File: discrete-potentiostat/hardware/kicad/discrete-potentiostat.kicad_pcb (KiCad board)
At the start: 6 copper layers, 26 x 24 mm, 70 parts, among them J1 ELECTRODES, J2 SWD, U1 BQ51013BRHLR, U2 MIC5205-3.3YM5, U3 nRF52832-QFAA, U4 OPA2391DGKR, U5 REF35102QDBVR, U6 MCP73832T-2ACI/OT, Y1 32MHz 8pF 10ppm

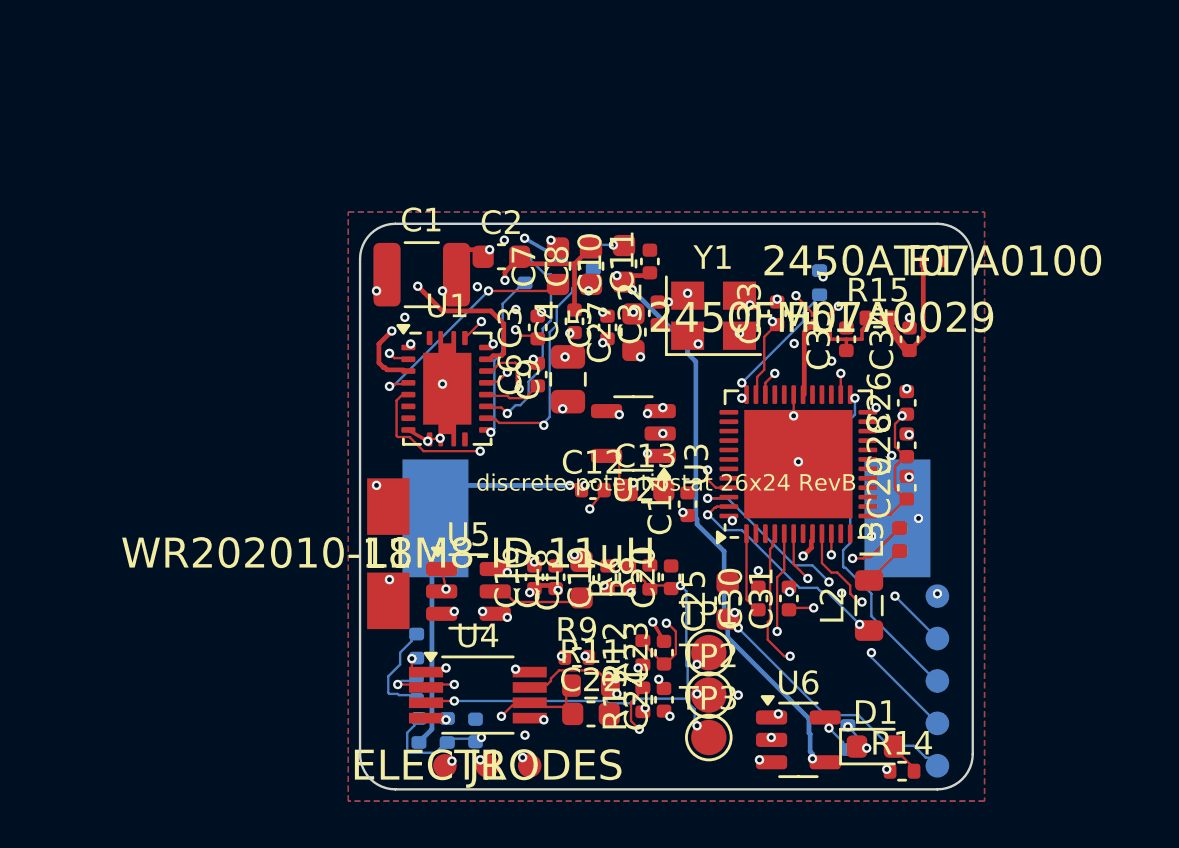
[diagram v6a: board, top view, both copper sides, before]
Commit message: Shrink board to 23.4x22mm (RevC, -17.5%); 4-layer ruled out
Size floor analysis: width bound by LIR2032 tab pads (+/-9.8mm + pad +
edge), height by the O21 cell zone -> 23.4x22 is the practical minimum
without changing the battery/tab structure.

- RevC placement: ICs on top; back reduced to 4 corner pockets (R1/R2/
  TH1, R3, R5/R6/C15); J2 SWD pads + TP1-3 moved to the front right
  column (clears the battery, easier soldering); DCDC inductors L2/L3
  relocated next to U3.46/47 (fixed the persistent DCC/DEC4 congestion);
  C30 rotated 180deg so DEC1 faces the open channel
- Routing: auto-route + priority/rip convergence to 4 links, then
  validated hand paths (close4.py): DCC via-in-pad U3.47 -> B detour ->
  via in L2.1; CLAMP2 B diagonal; DEC1 In3 + via-in-pad C30.1; ADC_P
  all-front channel route; +BATT/AFE_PWR/COMM1 local reroutes for GND
  orphan stitching
- Final DRC: 0 unconnected, 0 clearance, 0 hole, 0 edge, 0 isolated
- 4-layer experiment (same placement, 3 routing layers): fresh, priority
  and AGGRO strategies all plateau at 12-22 unconnected pads -> 6-layer
  stays; conclusion documented in kicad/README
- generator: gen_pcb.py is now the RevC generator (LAYERS4=1 for the 4L
  variant; legalize before RF pre-route), route_pcb.py gains PRIORITY/
  BOARD_W/H envs + 4L layer map fix; new gnd_fix_auto.py, finish_links.py,
  close4.py

Co-Authored-By: Claude Fable 5 <noreply@anthropic.com>
Claude-Session: https://claude.ai/code/session_01GUNJUwfGKqvkZFmTaLQRu3
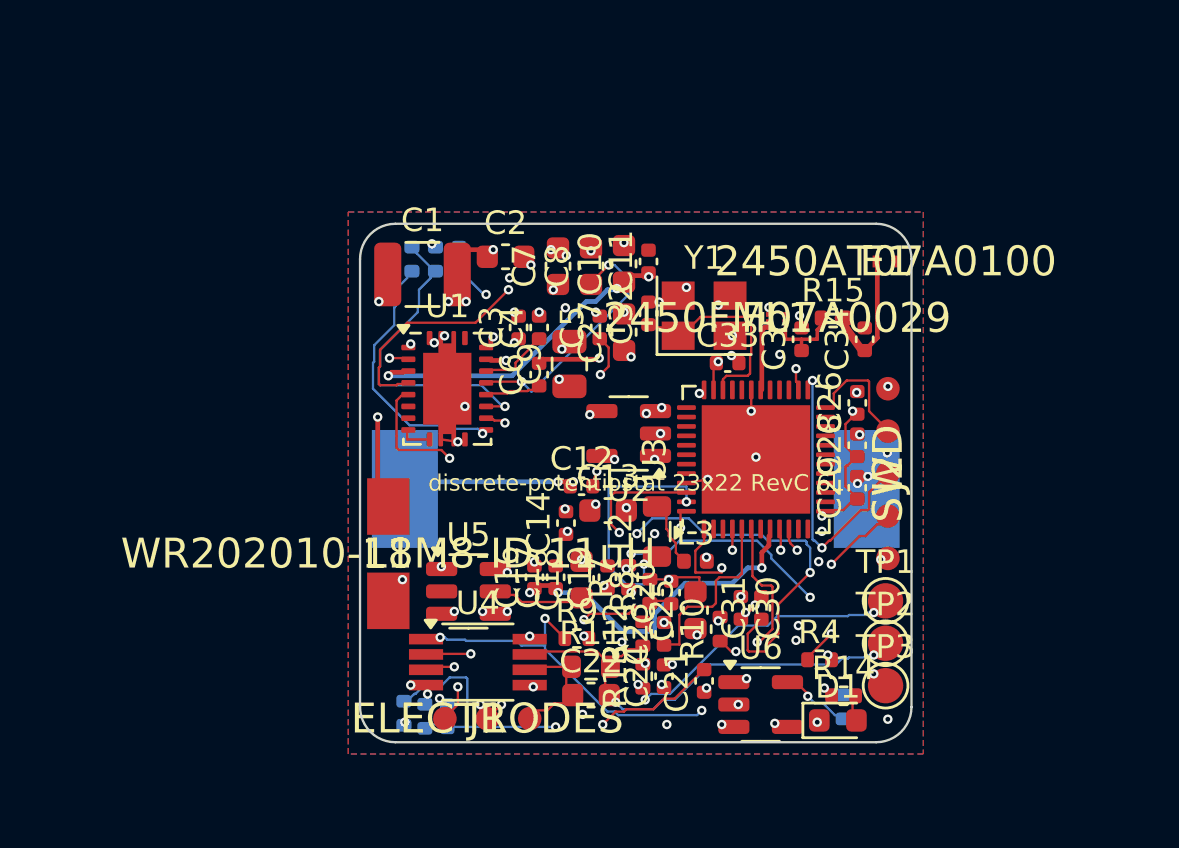
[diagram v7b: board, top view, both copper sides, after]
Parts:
- C21, J2, R10, R4: moved to F.Cu
- moved R4 16.0 mm to (119.5, 118.5), turned to 0 degrees
- moved R10 12.9 mm to (115.3, 117.2)
- moved C21 12.2 mm to (114.6, 119.4)
- moved L2 9.53 mm to (112.6, 113.1)
- moved J2 9.05 mm to (122.4, 110.6)
- moved L3 8.72 mm to (114.2, 114.3), turned to 0 degrees
- moved TP1 7.82 mm to (122.3, 116.0)
- moved TP2 7.82 mm to (122.3, 117.8)
- moved TP3 7.82 mm to (122.3, 119.6)
- moved TH1 5.70 mm to (104.2, 101.5)
- moved R2 5.32 mm to (103.2, 101.5)
- moved C14 5.22 mm to (108.7, 112.7)
- moved R1 4.83 mm to (102.2, 101.5)
- moved R14 4.05 mm to (120.5, 120.0)
- moved C33 2.98 mm to (115.6, 105.9), turned to 0 degrees
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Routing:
- net CE_AMP: track 5.83 -> 18.5 mm, vias 3 -> 4
- net CHG_N: track 20.9 -> 8.89 mm, vias 3 -> 4
- net RECT: track 15.0 -> 3.23 mm
- net DEC4: track 13.1 -> 24.3 mm
- net VBIAS: track 18.5 -> 27.5 mm, vias 3 -> 6
- net RE: track 5.55 -> 13.9 mm, vias 3 -> 4
- net TIA_OUT: track 8.26 -> 16.5 mm, vias 4 -> 2
- net VREF: track 17.3 -> 25.0 mm, vias 6 -> 7
- net ADC_N: track 15.8 -> 8.30 mm
- net +BATT: track 34.6 -> 41.4 mm, vias 7 -> 9
- net ADC_P: track 14.7 -> 8.04 mm, vias 3 -> 0
- net +3V3: track 44.7 -> 38.5 mm, vias 7 -> 10
- net NRST: track 10.6 -> 4.31 mm, vias 2 -> 0
- net V5OUT: track 38.2 -> 33.7 mm
- net CLAMP2: track 5.86 -> 10.4 mm
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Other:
- board size 26 x 24 mm -> 23.4 x 22 mm
- board text added: "discrete-potentiostat 23x22 RevC 6L"
- board text removed: "discrete-potentiostat 26x24 RevB"

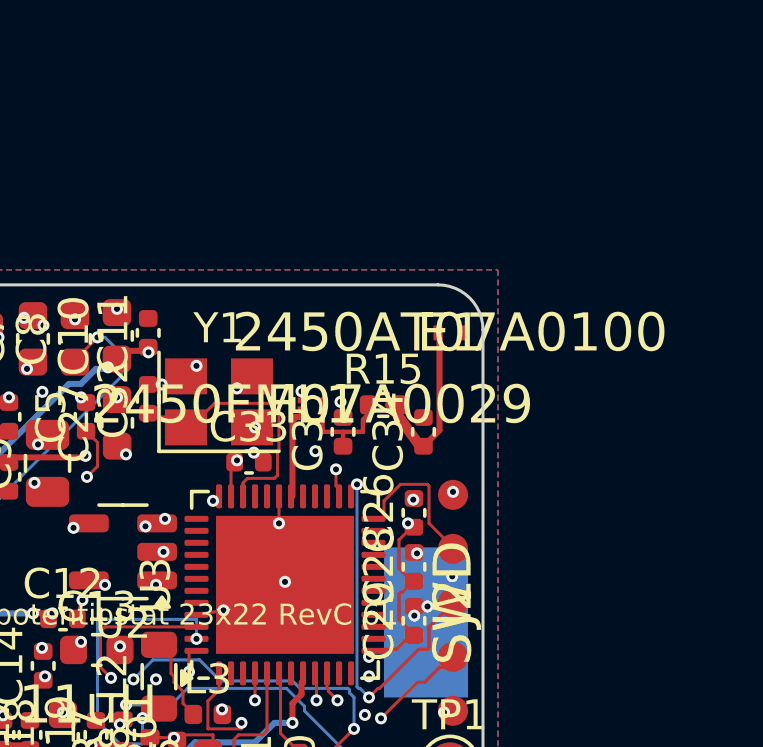
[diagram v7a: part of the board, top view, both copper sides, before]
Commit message: Fix E1 antenna to datasheet-true 4-terminal land pattern (GND connected)
Johanson 2450AT07A0100 datasheet (36S0021A Rev 4.1) defines 4 terminals:
1/4 = Feed, 2/3 = GND. Previous footprint was a wrong 2-pad guess with
the GND end floating.

- gen_pcb.py: 4-pad footprint (0.3x0.25 pads, rows +-0.3 along L,
  columns +-0.175 across W per eval-board land pattern); E1 moved to
  (19.4, 0.95) rot 270 - vertical edge mount, GND row toward top edge;
  parametric feed bridge to R15.2 and 0.3mm GND strip into left F pour
- gen_sch.py: custom 4-pin antenna symbol (1/4 ANT_FEED, 2/3 GND);
  netlist check PASS (47 nets)
- Board file: live surgery applied (new E1 + feed bridge + GND strip,
  old 2-pad E1 and stub removed); DRC re-verified - zero copper
  violations (unconnected 0, clearance 0)
- Schematic/PDFs regenerated; bom.md and kicad/README.md updated

Co-Authored-By: Claude Fable 5 <noreply@anthropic.com>
Claude-Session: https://claude.ai/code/session_01GUNJUwfGKqvkZFmTaLQRu3
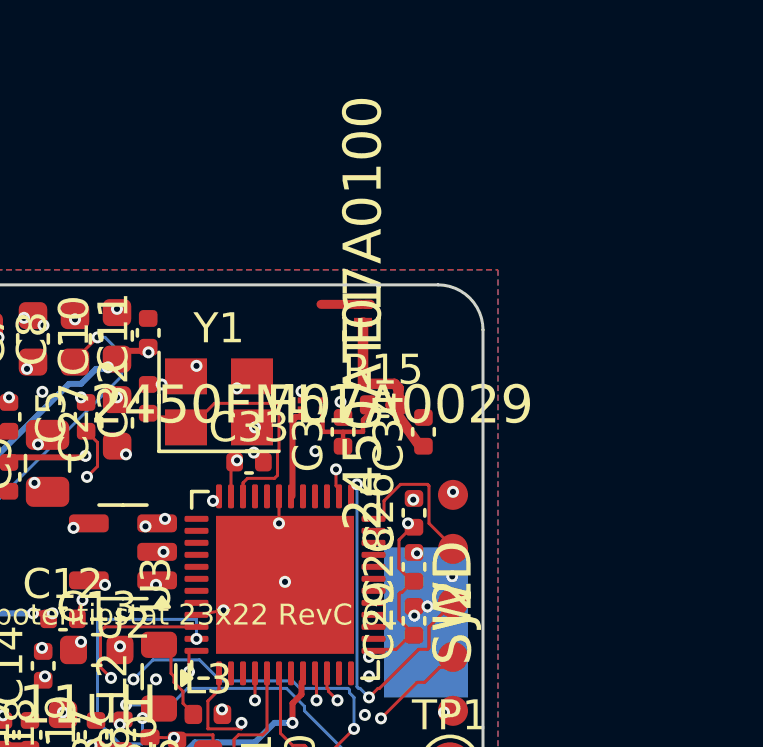
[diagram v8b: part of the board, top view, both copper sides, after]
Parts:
- moved E1 2.97 mm to (119.4, 101.0), turned to -90 degrees
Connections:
- E1 pad 2: (no net) -> GND
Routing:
- net GND: track 16.8 -> 18.4 mm
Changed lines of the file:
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@@
     )
   )
-  (footprint "pstat:Johanson_2450AT07A0100" (layer "F.Cu")
-    (at 122.3 101.6)
-    (fp_text reference "E1" (at 0 0) (layer "F.SilkS")
-        (effects (font (size 1.27 1.27) (thickness 0.15)))
-    )
-    (fp_text value "2450AT07A0100" (at 0 0) (layer "F.SilkS")
-        (effects (font (size 1.27 1.27) (thickness 0.15)))
-    )
-    (pad "1" smd rect (at -0.4 0) (size 0.3 0.5) (layers "F.Cu" "F.Paste" "F.Mask")
-      (net 10 "ANT_FEED") (thermal_bridge_angle 45))
-    (pad "2" smd rect (at 0.4 0) (size 0.3 0.5) (layers "F.Cu" "F.Paste" "F.Mask")
-      (thermal_bridge_angle 45))
-  )
   (footprint "C_0402_1005Metric" (layer "F.Cu")
     (at 121.1 109.4 90)
@@
     )
   )
+  (footprint "pstat:Johanson_2450AT07A0100" (layer "F.Cu")
+    (at 119.4 100.95 -90)
+    (fp_text reference "E1" (at 0 0 -90) (layer "F.SilkS")
+        (effects (font (size 1.27 1.27) (thickness 0.15)))
+    )
+    (fp_text value "2450AT07A0100" (at 0 0 -90) (layer "F.SilkS")
+        (effects (font (size 1.27 1.27) (thickness 0.15)))
+    )
+    (pad "1" smd rect (at 0.3 -0.175 270) (size 0.3 0.25) (layers "F.Cu" "F.Paste" "F.Mask")
+      (net 10 "ANT_FEED") (thermal_bridge_angle 45))
+    (pad "2" smd rect (at -0.3 -0.175 270) (size 0.3 0.25) (layers "F.Cu" "F.Paste" "F.Mask")
+      (net 28 "GND") (thermal_bridge_angle 45))
+    (pad "3" smd rect (at -0.3 0.175 270) (size 0.3 0.25) (layers "F.Cu" "F.Paste" "F.Mask")
+      (net 28 "GND") (thermal_bridge_angle 45))
+    (pad "4" smd rect (at 0.3 0.175 270) (size 0.3 0.25) (layers "F.Cu" "F.Paste" "F.Mask")
+      (net 10 "ANT_FEED") (thermal_bridge_angle 45))
+  )
   (footprint "pstat:Johanson_0402_4pin" (layer "F.Cu")
     (at 117.7 104)
@@
   (segment (start 118.735 105.38) (end 118.735 104.9) (width 0.15) (layer "F.Cu") (net 9))
   (segment (start 118.05 104.9) (end 119.4 104.9) (width 0.15) (layer "F.Cu") (net 9))
+  (segment (start 120.45 103.3) (end 120.585 103.44) (width 0.35) (layer "F.Cu") (net 10))
+  (segment (start 120.585 103.44) (end 120.585 103.9) (width 0.35) (layer "F.Cu") (net 10))
   (segment (start 120.31 104) (end 121.3 105.38) (width 0.35) (layer "F.Cu") (net 10))
-  (segment (start 121.95 104.845) (end 121.95 101.6) (width 0.2) (layer "F.Cu") (net 10))
-  (segment (start 121.415 105.38) (end 121.95 104.845) (width 0.2) (layer "F.Cu") (net 10))
+  (segment (start 119.4 103.3) (end 120.45 103.3) (width 0.35) (layer "F.Cu") (net 10))
+  (segment (start 119.4 101.25) (end 119.4 103.3) (width 0.35) (layer "F.Cu") (net 10))
   (segment (start 101.25 105.7) (end 101.85 105.7) (width 0.1) (layer "F.Cu") (net 11))
   (via (at 106.55 105.05) (size 0.4) (drill 0.2) (layers "F.Cu" "B.Cu") (net 11))
@@
   (segment (start 112.24 103.32) (end 112.69 103.32) (width 0.15) (layer "F.Cu") (net 28))
   (segment (start 111.299999 112.17) (end 111.3 112.05) (width 0.1) (layer "F.Cu") (net 28))
+  (segment (start 119.65 100.65) (end 118 100.65) (width 0.3) (layer "F.Cu") (net 28))
   (segment (start 103.4625 114.65) (end 103.45 114.55) (width 0.1) (layer "F.Cu") (net 28))
   (segment (start 102 108.75) (end 102 109.15) (width 0.1) (layer "F.Cu") (net 28))
